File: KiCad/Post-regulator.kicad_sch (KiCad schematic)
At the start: 111 parts, among them IC17 LTC2050HVCS8#PBF, IC18 TL072D, IC19 TL072D, IC20 SN74LVC1G3157DCKR, Q10 MMBT5401, Q11 MMBT5401, Q12 BCP56-16.115, Q13 MMBT5551, Q14 IRFP250NPBF, Q15 BCP56-16.115, Q16 BC857C, Q17 IRFI9Z34GPBF, Q18 PSMN0R9-25YLC, Q19 PSMN0R9-25YLC, Q9 MMBT5551

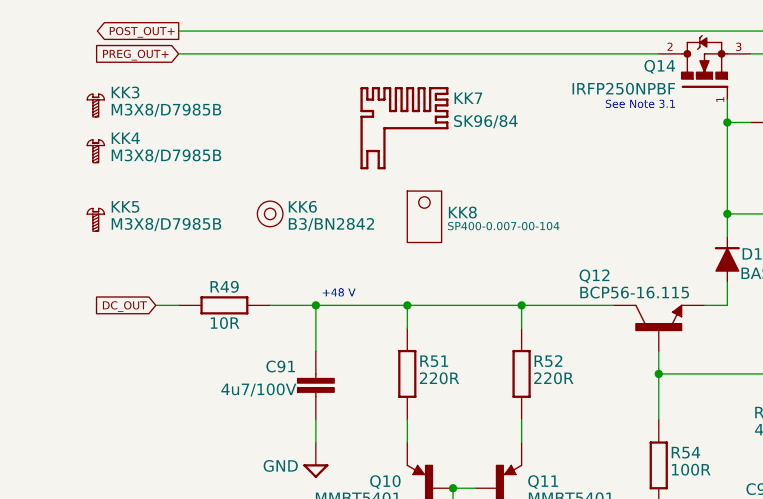
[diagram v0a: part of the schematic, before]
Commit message: DIB_MISO and DIB_MOSI swapped
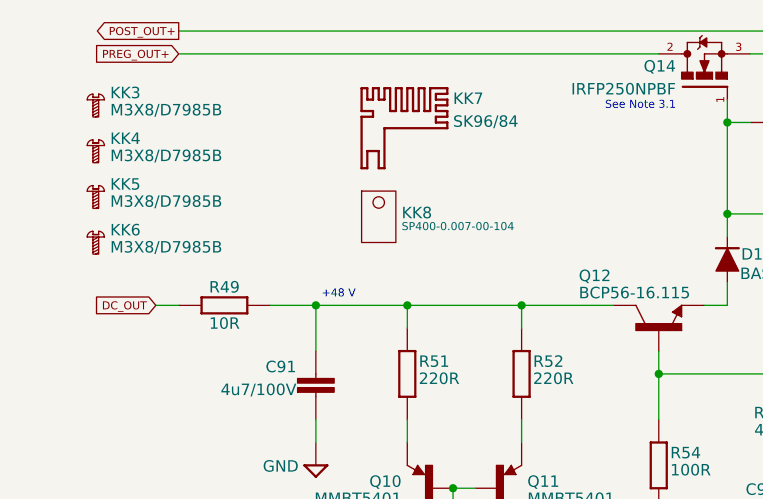
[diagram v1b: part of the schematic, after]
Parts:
- removed KK6: B3/BN2842, symbol PCM_EEZ_unsorted:B3/BN2842
- added KK6: M3X8/D7985B, symbol PCM_EEZ_unsorted:M3X8/D7985B
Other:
- moved on the sheet: KK5, KK8
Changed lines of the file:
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@@
 	(title_block
 		(title "${project_name}")
-		(date "2025-12-08")
+		(date "2025-12-17")
 		(rev "${project_version}")
 		(company "${project_creator}")
@@
 	)
 	(symbol
+		(lib_id "PCM_EEZ_unsorted:M3X8/D7985B")
+		(at 22.86 38.1 0)
+		(unit 1)
+		(exclude_from_sim no)
+		(in_bom yes)
+		(on_board no)
+		(dnp no)
+		(fields_autoplaced yes)
+		(property "Reference" "KK6"
+			(at 25.4 38.1 0)
+			(do_not_autoplace yes)
+			(effects
+				(font
+					(size 1.27 1.27)
+				)
+				(justify left bottom)
+			)
+		)
+		(property "Value" "M3X8/D7985B"
+			(at 25.4 40.005 0)
+			(do_not_autoplace yes)
+			(effects
+				(font
+					(size 1.27 1.27)
+				)
+				(justify left bottom)
+			)
+		)
+		(property "Footprint" ""
+			(at 22.86 38.1 0)
+			(effects
+				(font
+					(size 1.27 1.27)
+				)
+				(hide yes)
+			)
+		)
+		(property "Datasheet" ""
+			(at 22.86 38.1 0)
+			(effects
+				(font
+					(size 1.27 1.27)
+				)
+				(hide yes)
+			)
+		)
+		(property "Description" "Screw; M3x8; 0.5; Head: cheese head; Phillips; PH1; DIN 7985"
+			(at 22.86 40.64 0)
+			(effects
+				(font
+					(size 1.27 1.27)
+				)
+				(hide yes)
+			)
+		)
+		(property "DigiKey" "-"
+			(at 22.86 43.18 0)
+			(show_name yes)
+			(effects
+				(font
+					(size 1.27 1.27)
+				)
+				(hide yes)
+			)
+		)
+		(property "Mouser" "-"
+			(at 22.86 45.72 0)
+			(show_name yes)
+			(effects
+				(font
+					(size 1.27 1.27)
+				)
+				(hide yes)
+			)
+		)
+		(property "TME" "M3X8/D7985B"
+			(at 22.86 48.26 0)
+			(show_name yes)
+			(effects
+				(font
+					(size 1.27 1.27)
+				)
+				(hide yes)
+			)
+		)
+		(instances
+			(project "EEZ DIB DCP405plus"
+				(path "/65943c0e-8943-4d2a-93dc-fb4938f73312/34bb83a5-d559-4d80-b3e4-82ef079c17b9"
+					(reference "KK6")
+					(unit 1)
+				)
+			)
+		)
+	)
+	(symbol
 		(lib_id "PCM_EEZ_passives:C-EU")
 		(at 63.5 127 270)
@@
 	)
 	(symbol
-		(lib_id "PCM_EEZ_unsorted:B3/BN2842")
-		(at 43.18 35.56 0)
-		(unit 1)
-		(exclude_from_sim no)
-		(in_bom yes)
-		(on_board no)
-		(dnp no)
-		(property "Reference" "KK6"
-			(at 45.085 35.56 0)
-			(do_not_autoplace yes)
-			(effects
-				(font
-					(size 1.27 1.27)
-				)
-				(justify left bottom)
-			)
-		)
-		(property "Value" "B3/BN2842"
-			(at 45.085 37.465 0)
-			(do_not_autoplace yes)
-			(effects
-				(font
-					(size 1.27 1.27)
-				)
-				(justify left bottom)
-			)
-		)
-		(property "Footprint" ""
-			(at 43.18 35.56 0)
-			(effects
-				(font
-					(size 1.27 1.27)
-				)
-				(hide yes)
-			)
-		)
-		(property "Datasheet" ""
-			(at 43.18 35.56 0)
-			(effects
-				(font
-					(size 1.27 1.27)
-				)
-				(hide yes)
-			)
-		)
-		(property "Description" "Washer; externally serrated; M3"
-			(at 43.18 38.1 0)
-			(effects
-				(font
-					(size 1.27 1.27)
-				)
-				(hide yes)
-			)
-		)
-		(property "DigiKey" "-"
-			(at 43.18 40.64 0)
-			(show_name yes)
-			(effects
-				(font
-					(size 1.27 1.27)
-				)
-				(hide yes)
-			)
-		)
-		(property "Mouser" "-"
-			(at 43.18 43.18 0)
-			(show_name yes)
-			(effects
-				(font
-					(size 1.27 1.27)
-				)
-				(hide yes)
-			)
-		)
-		(property "TME" "B3/BN2842"
-			(at 43.18 45.72 0)
-			(show_name yes)
-			(effects
-				(font
-					(size 1.27 1.27)
-				)
-				(hide yes)
-			)
-		)
-		(instances
-			(project ""
-				(path "/65943c0e-8943-4d2a-93dc-fb4938f73312/34bb83a5-d559-4d80-b3e4-82ef079c17b9"
-					(reference "KK6")
-					(unit 1)
-				)
-			)
-		)
-	)
-	(symbol
 		(lib_id "PCM_EEZ_passives:R-EU")
 		(at 142.24 149.86 270)
@@
 	(symbol
 		(lib_id "PCM_EEZ_unsorted:TO247_Thermal_pad")
-		(at 58.42 33.02 0)
+		(at 53.34 33.02 0)
 		(unit 1)
 		(exclude_from_sim no)
@@
 		(fields_autoplaced yes)
 		(property "Reference" "KK8"
-			(at 62.865 36.195 0)
+			(at 57.785 36.195 0)
 			(do_not_autoplace yes)
 			(effects
@@
 		)
 		(property "Value" "SP400-0.007-00-104"
-			(at 62.865 37.465 0)
+			(at 57.785 37.465 0)
 			(do_not_autoplace yes)
 			(effects
@@
 		)
 		(property "Footprint" ""
-			(at 58.42 33.02 0)
+			(at 53.34 33.02 0)
 			(effects
 				(font
@@
 		)
 		(property "Datasheet" ""
-			(at 58.42 33.02 0)
+			(at 53.34 33.02 0)
 			(effects
 				(font
@@
 		)
 		(property "Description" ""
-			(at 58.42 33.02 0)
+			(at 53.34 33.02 0)
 			(effects
 				(font
@@
 		)
 		(property "DigiKey" "BER204-ND"
-			(at 58.42 40.64 0)
+			(at 53.34 40.64 0)
 			(show_name yes)
 			(effects
@@
 		)
 		(property "Mouser" "951-SP400-007-00-104"
-			(at 58.42 43.18 0)
+			(at 53.34 43.18 0)
 			(show_name yes)
 			(effects
@@
 	(symbol
 		(lib_id "PCM_EEZ_unsorted:M3X8/D7985B")
-		(at 22.86 35.56 0)
+		(at 22.86 33.02 0)
 		(unit 1)
 		(exclude_from_sim no)
@@
 		(fields_autoplaced yes)
 		(property "Reference" "KK5"
-			(at 25.4 35.56 0)
+			(at 25.4 33.02 0)
 			(do_not_autoplace yes)
 			(effects
@@
 		)
 		(property "Value" "M3X8/D7985B"
-			(at 25.4 37.465 0)
+			(at 25.4 34.925 0)
 			(do_not_autoplace yes)
 			(effects
@@
 		)
 		(property "Footprint" ""
-			(at 22.86 35.56 0)
+			(at 22.86 33.02 0)
 			(effects
 				(font
@@
 		)
 		(property "Datasheet" ""
-			(at 22.86 35.56 0)
+			(at 22.86 33.02 0)
 			(effects
 				(font
@@
 		)
 		(property "Description" "Screw; M3x8; 0.5; Head: cheese head; Phillips; PH1; DIN 7985"
-			(at 22.86 38.1 0)
+			(at 22.86 35.56 0)
 			(effects
 				(font
@@
 		)
 		(property "DigiKey" "-"
-			(at 22.86 40.64 0)
+			(at 22.86 38.1 0)
 			(show_name yes)
 			(effects
@@
 		)
 		(property "Mouser" "-"
-			(at 22.86 43.18 0)
+			(at 22.86 40.64 0)
 			(show_name yes)
 			(effects
@@
 		)
 		(property "TME" "M3X8/D7985B"
-			(at 22.86 45.72 0)
+			(at 22.86 43.18 0)
 			(show_name yes)
 			(effects
